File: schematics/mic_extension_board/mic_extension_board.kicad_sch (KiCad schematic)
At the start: 56 parts, among them J1 XLR3, J2 Power, J3 Aux In, J4 I2C Bus, J5 6Pin ISP, J6 Input/Output, J7 XLR3, J8 XLR3, SW1 Stompbutton 1, SW2 Stompbutton 2, SW3 Stompbutton 3, U1 TL074, U2 TL072, U3 APE8865N-33-HF-3, U4 NE5534, U5 ATmega88A-A, U6 24LC128

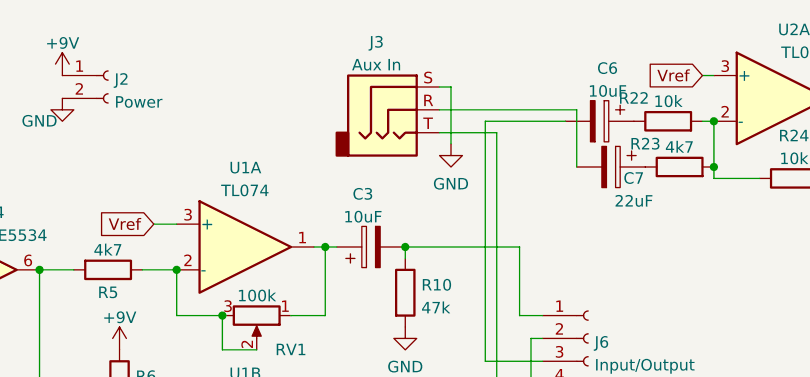
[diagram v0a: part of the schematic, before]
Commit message: corrected ic footprints, shrinked
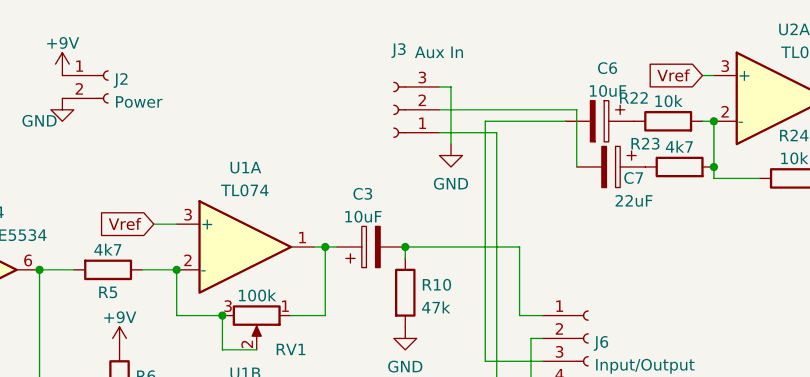
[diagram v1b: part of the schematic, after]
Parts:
- removed J3: Aux In, Connector_Audio:Jack_3.5mm_CUI_SJ-3523-SMT_Horizontal, symbol Connector:AudioJack3
- added J3: Aux In, Connector_PinHeader_2.54mm:PinHeader_1x03_P2.54mm_Vertical, symbol Connector:Conn_01x03_Female
- J1: footprint Connector_Audio:Jack_XLR_Neutrik_NC3FAAH-0_Horizontal -> Connector_PinHeader_2.54mm:PinHeader_1x03_P2.54mm_Vertical
- J7, J8: footprint Connector_Audio:Jack_XLR_Neutrik_NC3FAAH1-0_Horizontal -> Connector_PinHeader_2.54mm:PinHeader_1x03_P2.54mm_Vertical
- U1: footprint Package_SO:SO-14_5.3x10.2mm_P1.27mm -> Package_SO:SOIC-14_3.9x8.7mm_P1.27mm
- U2, U4, U6: footprint Package_SO:SO-8_5.3x6.2mm_P1.27mm -> Package_SO:SOIC-8_3.9x4.9mm_P1.27mm
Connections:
- net GND: now also J3.3 (Pin_3)
- net at C7.2: now also J3.2 (Pin_2)
- net at C5.2: now also J3.1 (Pin_1)

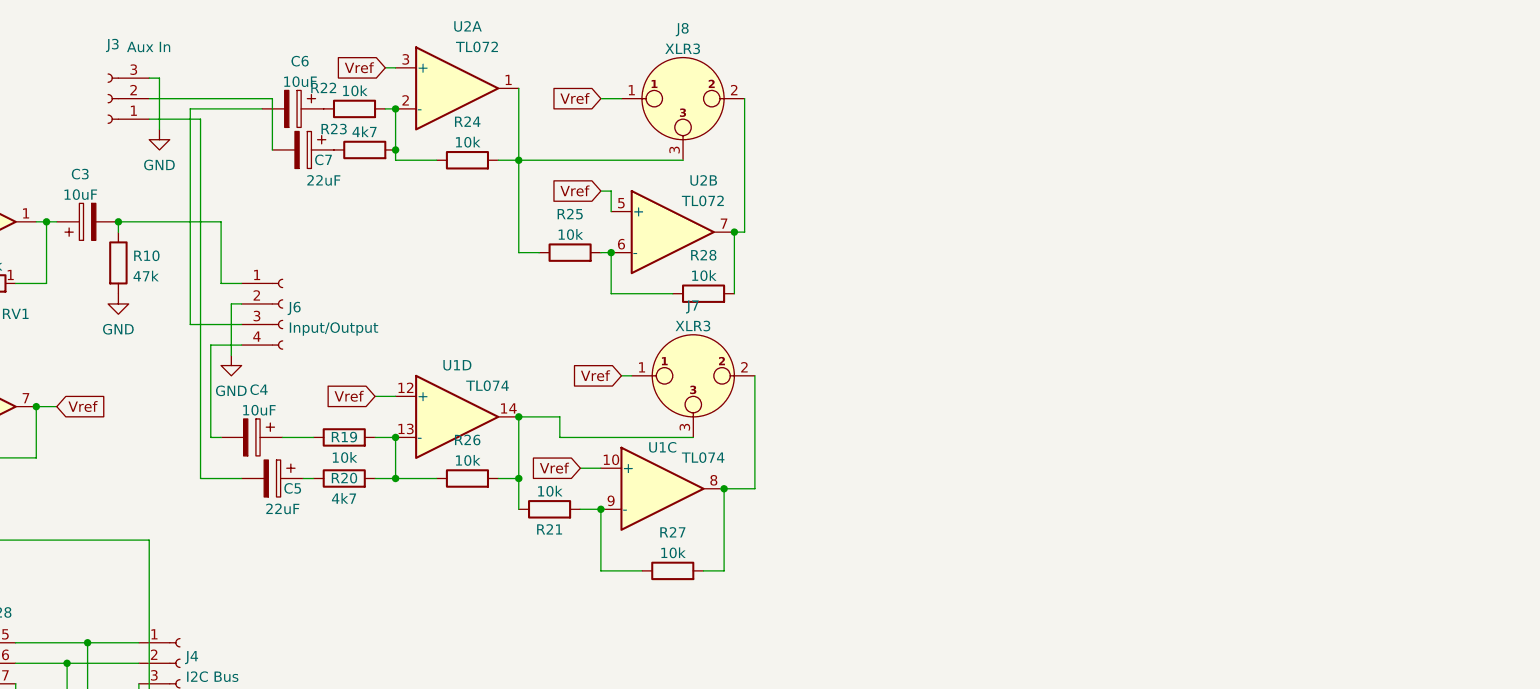
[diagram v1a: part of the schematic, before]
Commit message: added headphone amp
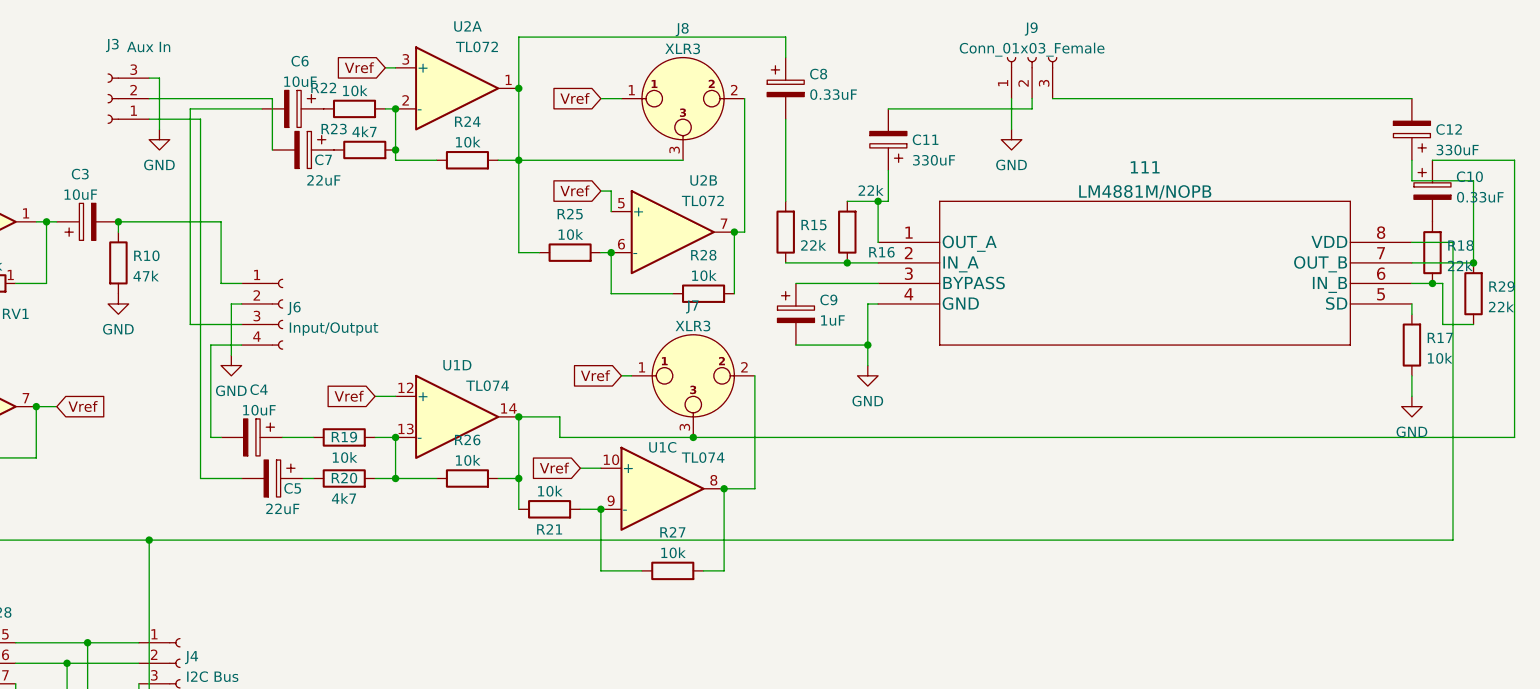
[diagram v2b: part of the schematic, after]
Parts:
- added 111: LM4881M/NOPB, Package_SO:SOIC-8_3.9x4.9mm_P1.27mm, symbol 2023-02-24_23-31-36:LM4881M/NOPB
- added C10, C8: 0.33uF, Capacitor_SMD:CP_Elec_4x4.5, symbol Device:C_Polarized
- added C11, C12: 330uF, Capacitor_SMD:CP_Elec_8x10.5, symbol Device:C_Polarized
- added C9: 1uF, Capacitor_SMD:CP_Elec_4x4.5, symbol Device:C_Polarized
- added J9: Conn_01x03_Female, Connector_PinHeader_2.54mm:PinHeader_1x03_P2.54mm_Vertical, symbol Connector:Conn_01x03_Female
- added R15, R16, R18, R29: 22k, Resistor_SMD:R_0603_1608Metric_Pad0.98x0.95mm_HandSolder, symbol Device:R
- added R17: 10k, Resistor_SMD:R_0603_1608Metric_Pad0.98x0.95mm_HandSolder, symbol Device:R
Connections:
- net GND: now also 111.4 (GND), C9.2, J9.1 (Pin_1), R17.1
- net at C2.1, J5.2 (Pin_2), R9.1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: now also 111.8 (VDD)
- net at J8.3, R24.2, R25.1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: now also C8.1
- net at J7.3, R21.1, R26.2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: now also C10.1
- new net: 111.6 (IN_B), R18.1, R29.1
- new net: C10.2, R18.2
- new net: 111.1 (OUT_A), C11.1, R16.2
- new net: 111.2 (IN_A), R15.1, R16.1
- new net: 111.3 (BYPASS), C9.1
- new net: 111.5 (SD), R17.2
- new net: 111.7 (OUT_B), C12.1, R29.2
- new net: C11.2, J9.2 (Pin_2)
- new net: C8.2, R15.2
- new net: C12.2, J9.3 (Pin_3)

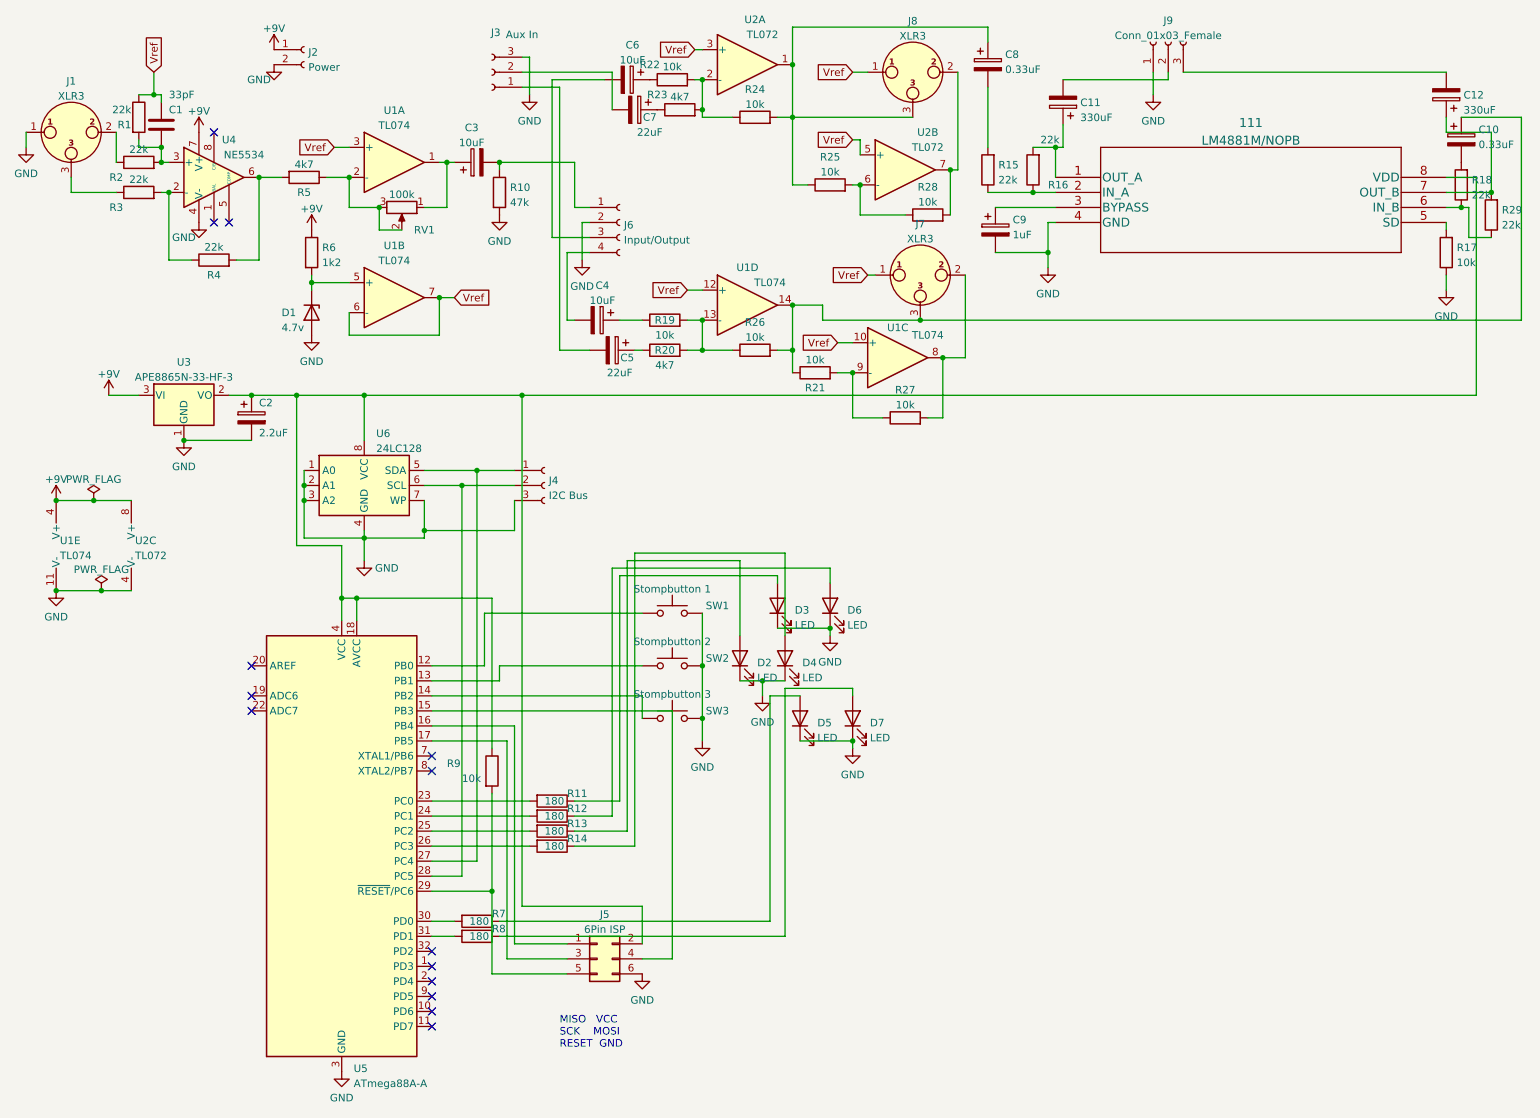
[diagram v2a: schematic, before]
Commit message: update mic expansion board
the design is now symmetric to the greatest extent, reduces cost
and nasty switch on/off behaviour
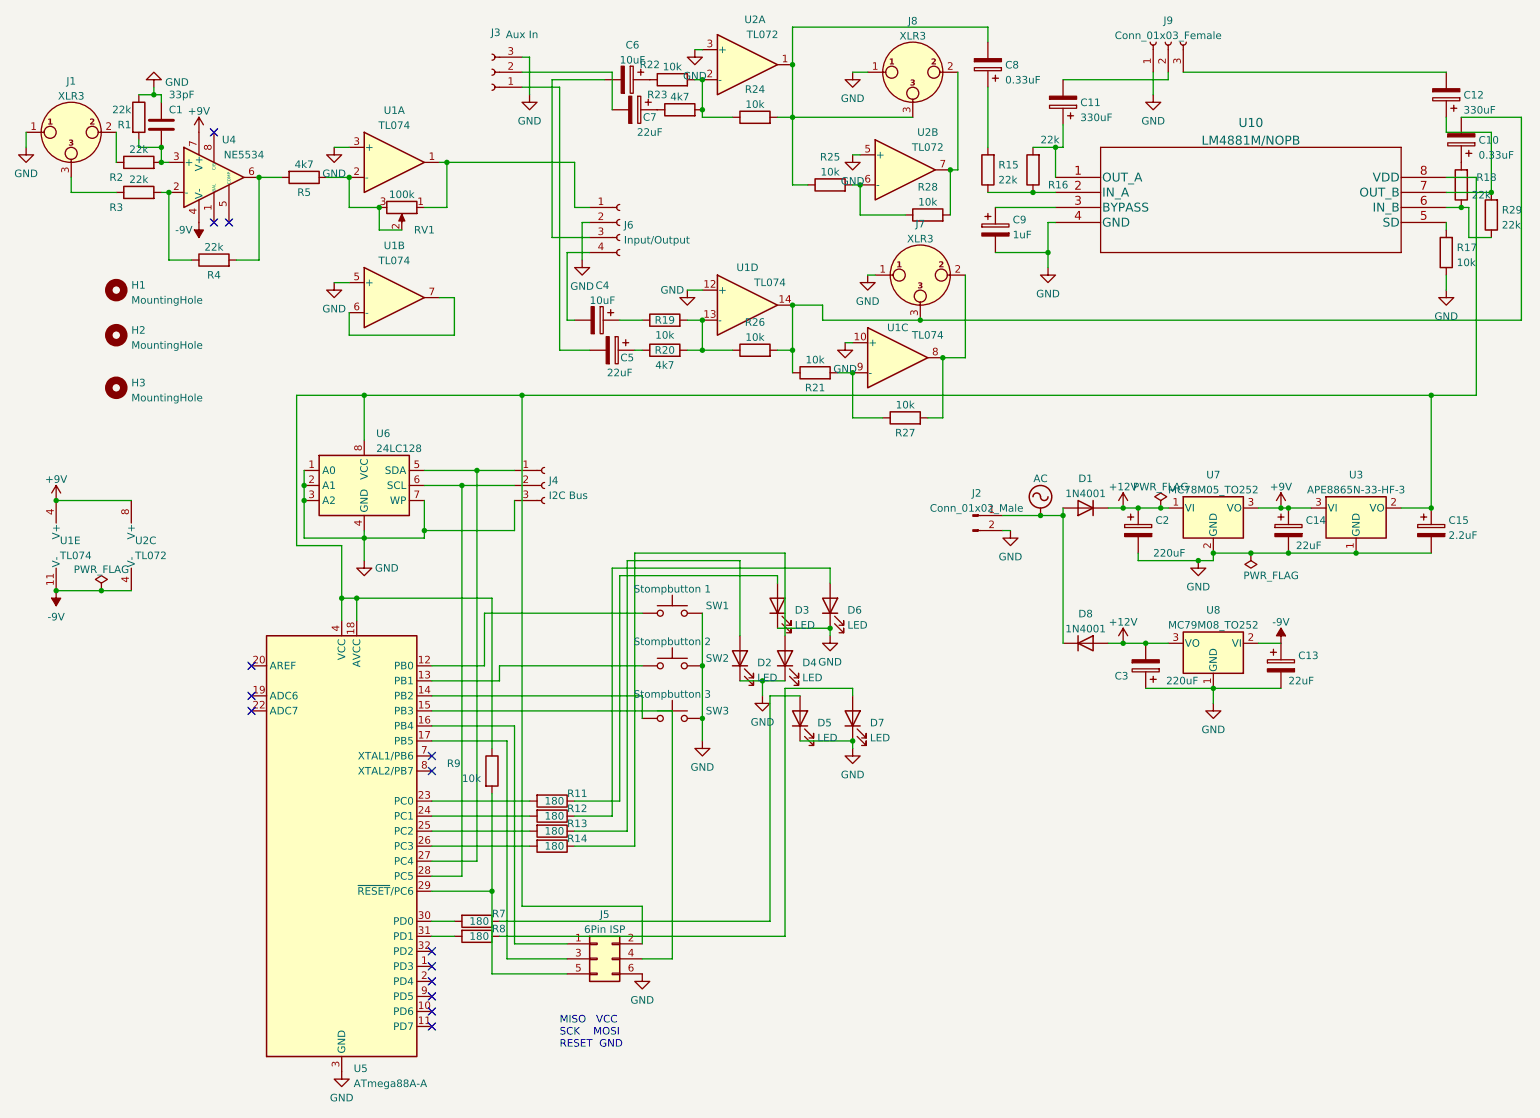
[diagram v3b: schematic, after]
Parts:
- removed D1: 4.7v, Diode_SMD:D_MiniMELF_Handsoldering, symbol Device:D_Zener
- removed J2: Power, Connector_PinHeader_2.54mm:PinHeader_1x02_P2.54mm_Vertical, symbol Connector:Conn_01x02_Female
- removed R10: 47k, Resistor_SMD:R_0603_1608Metric_Pad0.98x0.95mm_HandSolder, symbol Device:R
- removed R6: 1k2, Resistor_SMD:R_0603_1608Metric_Pad0.98x0.95mm_HandSolder, symbol Device:R
- added C13, C14: 22uF, Capacitor_SMD:CP_Elec_4x4.5, symbol Device:C_Polarized
- added C15: 2.2uF, Capacitor_SMD:CP_Elec_4x4.5, symbol Device:C_Polarized
- added D1, D8: 1N4001, Diode_THT:D_DO-41_SOD81_P10.16mm_Horizontal, symbol Diode:1N4001
- added H1, H2, H3: MountingHole, MountingHole:MountingHole_3.2mm_M3, symbol Mechanical:MountingHole
- added J2: Conn_01x02_Male, Connector_PinHeader_2.54mm:PinHeader_1x02_P2.54mm_Vertical, symbol Connector:Conn_01x02_Male
- added U7: MC78M05_TO252, Package_TO_SOT_SMD:TO-252-2, symbol Regulator_Linear:MC78M05_TO252
- added U8: MC79M08_TO252, Package_TO_SOT_SMD:TO-252-2, symbol Regulator_Linear:MC79M08_TO252
- C11, C12: footprint Capacitor_SMD:CP_Elec_8x10.5 -> Capacitor_SMD:CP_Elec_6.3x7.7
- C2: value 2.2uF -> 220uF; footprint Capacitor_SMD:CP_Elec_4x4.5 -> Capacitor_SMD:CP_Elec_6.3x7.7
- C3: value 10uF -> 220uF; footprint Capacitor_SMD:CP_Elec_4x4.5 -> Capacitor_SMD:CP_Elec_6.3x7.7
- renumbered 111 to U10
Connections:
- net +9V: now also C14.1, U7.3 (VO)
- net GND: now also C1.1, C3.1, J7.1, J8.1, R1.1, U1.10 (+), U1.12 (+), U1.3 (+), U1.5 (+), U2.3 (+), U2.5 (+), C13.2, C14.2, C15.2, J2.2 (Pin_2), U7.2 (GND), U8.1 (GND); no longer U1.11 (V-), U2.4 (V-), U4.4 (V-)
- net at R18.2: now also C10.1; no longer C10.2
- net at J5.2 (Pin_2), R9.1, U10.8 (VDD)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: now also C15.1; no longer C2.1
- net at J8.3, R24.2, R25.1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: now also C8.2; no longer C8.1
- net at J7.3, R21.1, R26.2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: now also C10.2; no longer C10.1
- net at J6.1 (Pin_1): now also RV1.1, U1.1; no longer C3.2
- net at R15.2: now also C8.1; no longer C8.2
- removed net Vref: C1.1, J7.1, J8.1, R1.1, U1.10 (+), U1.12 (+), U1.3 (+), U1.6 (-), U1.7, U2.3 (+), U2.5 (+)
- new net: U1.6 (-), U1.7
- new net +12V: C2.1, C3.2, D1.1 (K), D8.2 (A), U7.1 (VI), U8.3 (VO)
- new net -9V: C13.1, U1.11 (V-), U2.4 (V-), U4.4 (V-), U8.2 (VI)
- new net AC: D1.2 (A), D8.1 (K), J2.1 (Pin_1)
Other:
- moved on the sheet: C10, C8, U3

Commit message: last changes before order
* fixed last minor details
* tidied gitignore files
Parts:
- removed C4, C6: 10uF, Capacitor_SMD:CP_Elec_4x4.5, symbol Device:C_Polarized
- removed C5, C7: 22uF, Capacitor_SMD:CP_Elec_4x4.5, symbol Device:C_Polarized
- added J10: Conn_01x01_Male, Connector_PinHeader_2.54mm:PinHeader_1x01_P2.54mm_Vertical, symbol Connector:Conn_01x01_Male
- added TP1, TP2, TP3: TestPoint, TestPoint:TestPoint_Pad_D1.5mm, symbol Connector:TestPoint
- J5: footprint Connector_PinHeader_1.27mm:PinHeader_2x03_P1.27mm_Vertical -> Connector_PinHeader_2.54mm:PinHeader_2x03_P2.54mm_Vertical
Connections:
- net +9V: no longer U3.3 (VI)
- net -9V: now also C13.2; no longer C13.1
- net GND: now also C13.1; no longer C13.2
- net at U4.1 (BAL): now also TP2.1
- net at U4.5 (COMP): now also TP3.1
- net at U4.8 (C/B): now also TP1.1
- net at R19.1: now also J6.4 (Pin_4)
- net at R20.1: now also J3.1 (Pin_1)
- net at R22.1: now also J6.3 (Pin_3)
- net at R23.1: now also J3.2 (Pin_2)
- new net: J10.1 (Pin_1), U3.3 (VI)
- no-connect marks 14 -> 11
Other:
- moved on the sheet: C13, C14, R4

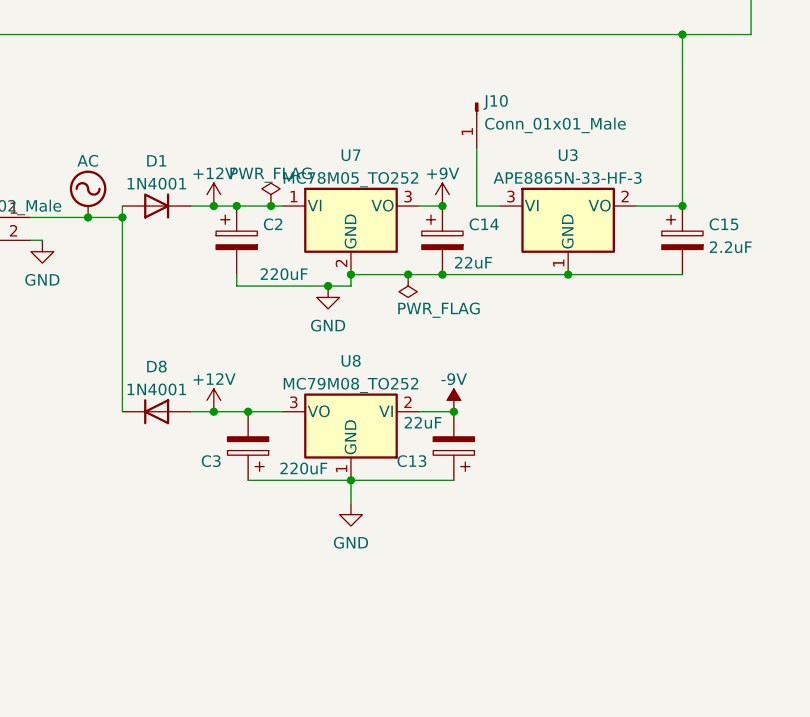
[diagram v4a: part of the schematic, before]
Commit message: expansio board firmware
* added settings for avr gcc
* fixed minor bug
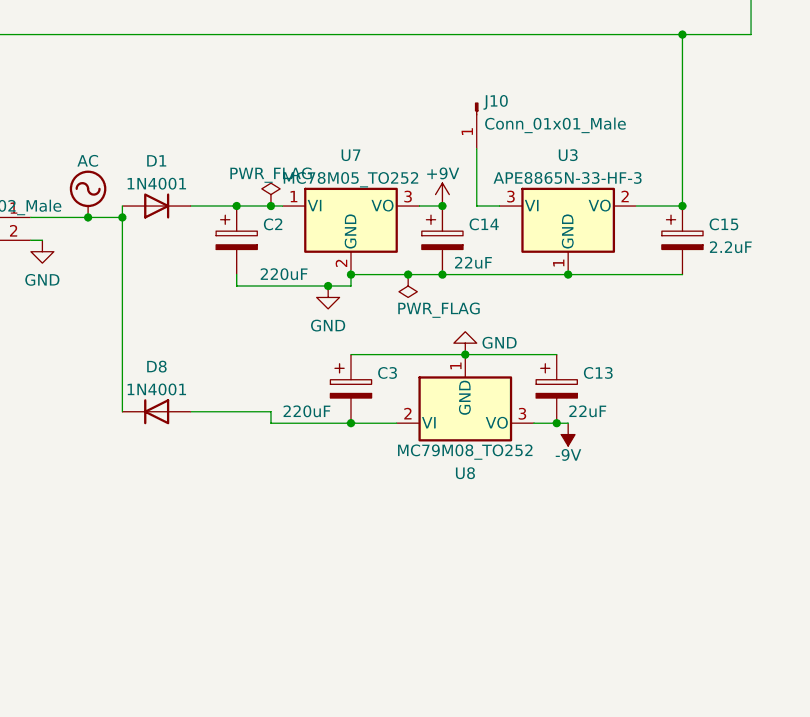
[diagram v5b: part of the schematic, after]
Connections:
- net -9V: now also U8.3 (VO); no longer U8.2 (VI)
- net +12V: no longer names the net of C2.1, D1.1 (K), U7.1 (VI)
- net +12V: no longer C3.2, D8.2 (A), U8.3 (VO)
- new net: C3.2, D8.2 (A), U8.2 (VI)
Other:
- moved on the sheet: C13, C3, U8
